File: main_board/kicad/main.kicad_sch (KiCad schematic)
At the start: 5 parts, among them J2 Motorbuchse, J3 Motorbuchse, J4 Batteriebuchse, J5 Conn_02x07_Odd_Even

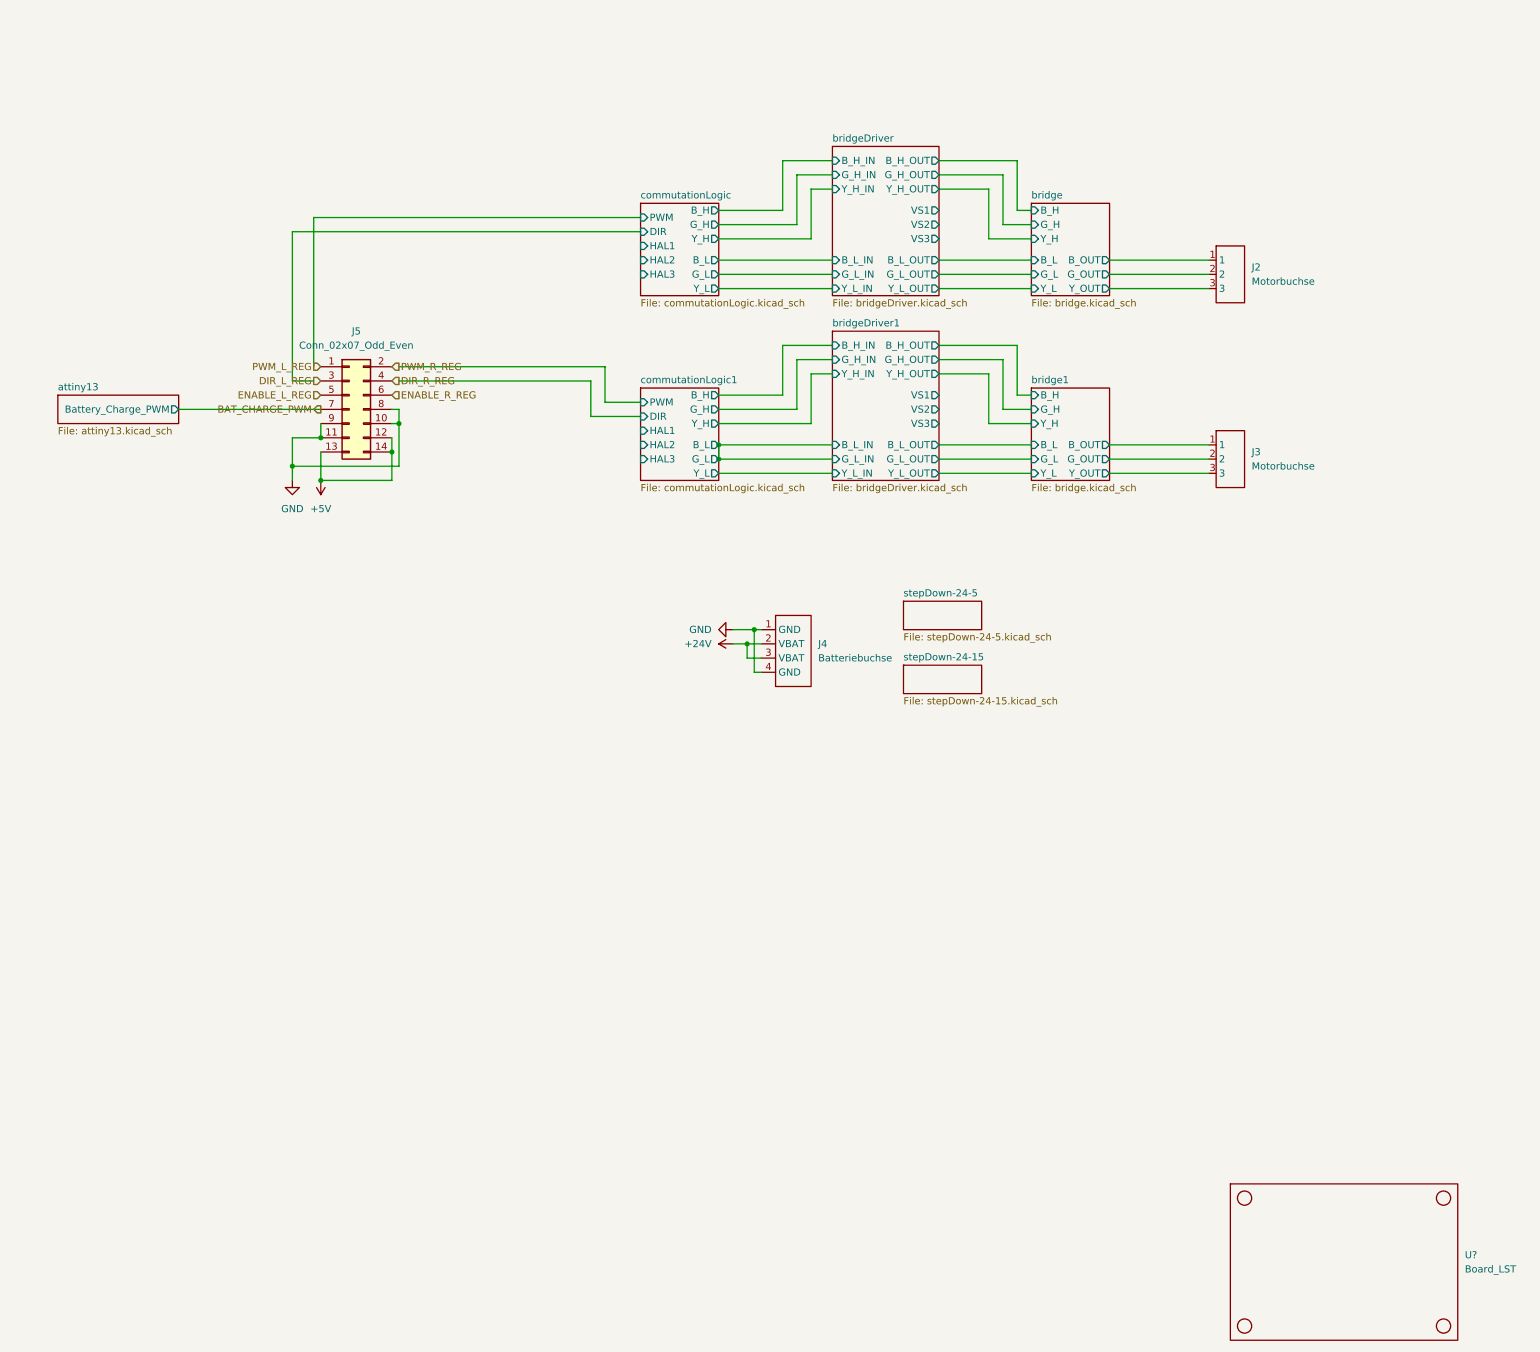
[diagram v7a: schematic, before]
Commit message: revamped root and bridge
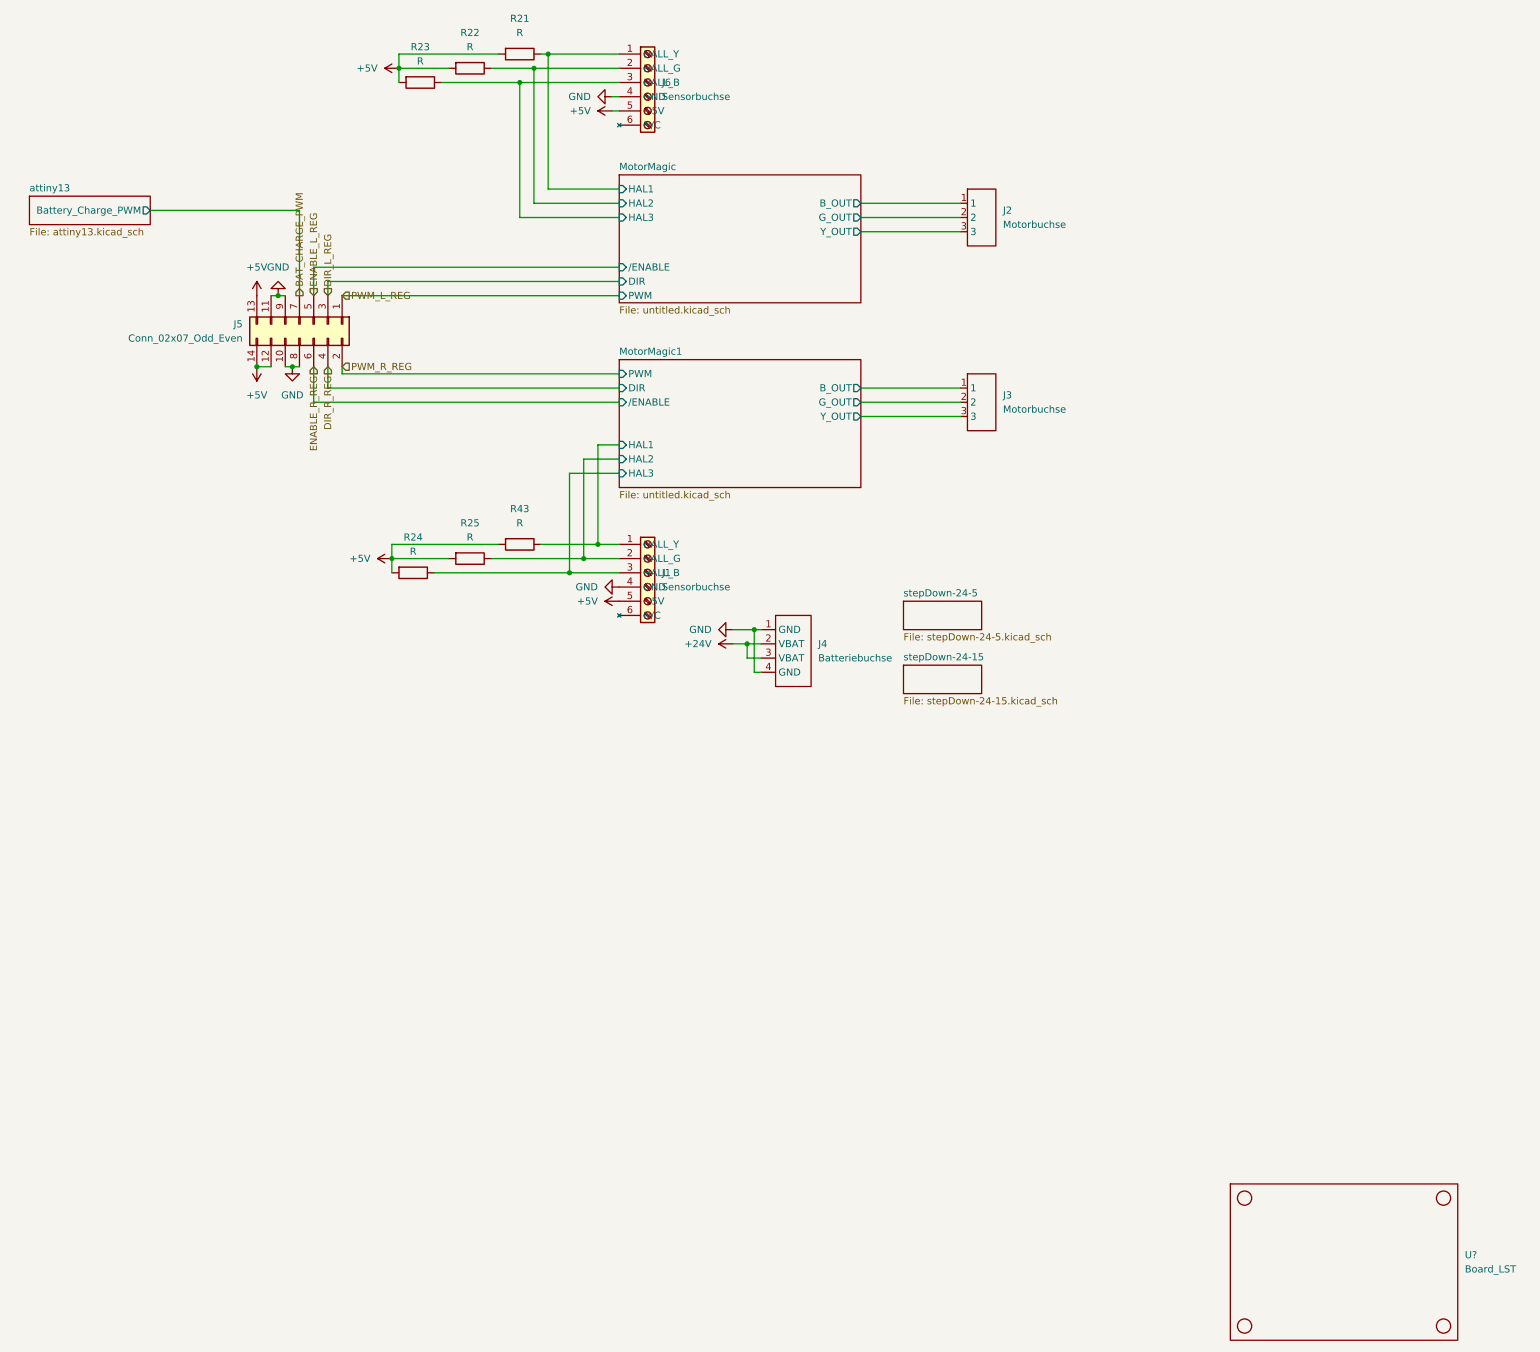
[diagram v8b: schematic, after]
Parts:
- added J1, J6: Sensorbuchse, Connector_Phoenix_MC:PhoenixContact_MC_1,5_6-G-3.81_1x06_P3.81mm_Horizontal, symbol 2022-lsd:Sensorbuchse
- added R21, R22, R23, R24, R25, R43: R, symbol Device:R
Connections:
- net +5V: now also J1.5 (+5V), J6.5 (+5V), R21.2, R22.2, R23.2, R24.2, R25.2, R43.2
- net GND: now also J1.4 (GND), J6.4 (GND)
- net bridge/B_OUT renamed MotorMagic/B_OUT
- net bridge/G_OUT renamed MotorMagic/G_OUT
- net bridge/Y_OUT renamed MotorMagic/Y_OUT
- net bridge1/B_OUT renamed MotorMagic1/B_OUT
- net bridge1/G_OUT renamed MotorMagic1/G_OUT
- net bridge1/Y_OUT renamed MotorMagic1/Y_OUT
- new net MotorMagic/HAL1: J6.1 (HALL_Y), R21.1
- new net MotorMagic/HAL2: J6.2 (HALL_G), R22.1
- new net MotorMagic/HAL3: J6.3 (HALL_B), R23.1
- new net MotorMagic1/HAL1: J1.1 (HALL_Y), R43.1
- new net MotorMagic1/HAL2: J1.2 (HALL_G), R25.1
- new net MotorMagic1/HAL3: J1.3 (HALL_B), R24.1
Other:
- removed sheet bridge
- removed sheet bridge1
- removed sheet bridgeDriver
- removed sheet bridgeDriver1
- removed sheet commutationLogic
- removed sheet commutationLogic1
- added sheet MotorMagic (untitled.kicad_sch)
- added sheet MotorMagic1 (untitled.kicad_sch)
- moved on the sheet: J2, J3, J5
